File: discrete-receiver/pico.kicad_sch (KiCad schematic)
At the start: 38 parts, among them SW1 Reset, U6 RP2350A, U7 W25Q128JVS, U8 NCP1117-3.3_SOT223, Y1 ABM8-272-T3

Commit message: update schematic for peter
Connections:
- net Pico_USB_D+ renamed Pico_USB+
- net Pico_USB_D- renamed Pico_USB-
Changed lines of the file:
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@@
-		)
-	)
-	(global_label "Pico_USB_D+"
-		(shape bidirectional)
-		(at 270.51 67.31 0)
-		(fields_autoplaced yes)
-		(effects
-			(font
-				(size 1.27 1.27)
-				(thickness 0.1588)
-			)
-			(justify left)
-		)
-		(property "Intersheetrefs" "${INTERSHEET_REFS}"
-			(at 287.3065 67.31 0)
-			(hide yes)
-			(show_name no)
-			(do_not_autoplace no)
-			(effects
-				(font
-					(size 1.27 1.27)
-				)
-				(justify left)
-			)
 		)
 	)
@@
 		)
 	)
-	(global_label "Pico_USB_D-"
-		(shape bidirectional)
-		(at 270.51 69.85 0)
-		(fields_autoplaced yes)
-		(effects
-			(font
-				(size 1.27 1.27)
-				(thickness 0.1588)
-			)
-			(justify left)
-		)
-		(property "Intersheetrefs" "${INTERSHEET_REFS}"
-			(at 287.3065 69.85 0)
-			(hide yes)
-			(show_name no)
-			(do_not_autoplace no)
-			(effects
-				(font
-					(size 1.27 1.27)
-				)
-				(justify left)
-			)
-		)
-	)
 	(global_label "XIN"
 		(shape passive)
@@
 		)
 	)
+	(hierarchical_label "Pico_USB+"
+		(shape output)
+		(at 270.51 67.31 0)
+		(effects
+			(font
+				(size 1.27 1.27)
+			)
+			(justify left)
+		)
+	)
+	(hierarchical_label "Pico_USB-"
+		(shape output)
+		(at 270.51 69.85 0)
+		(effects
+			(font
+				(size 1.27 1.27)
+			)
+			(justify left)
+		)
+	)

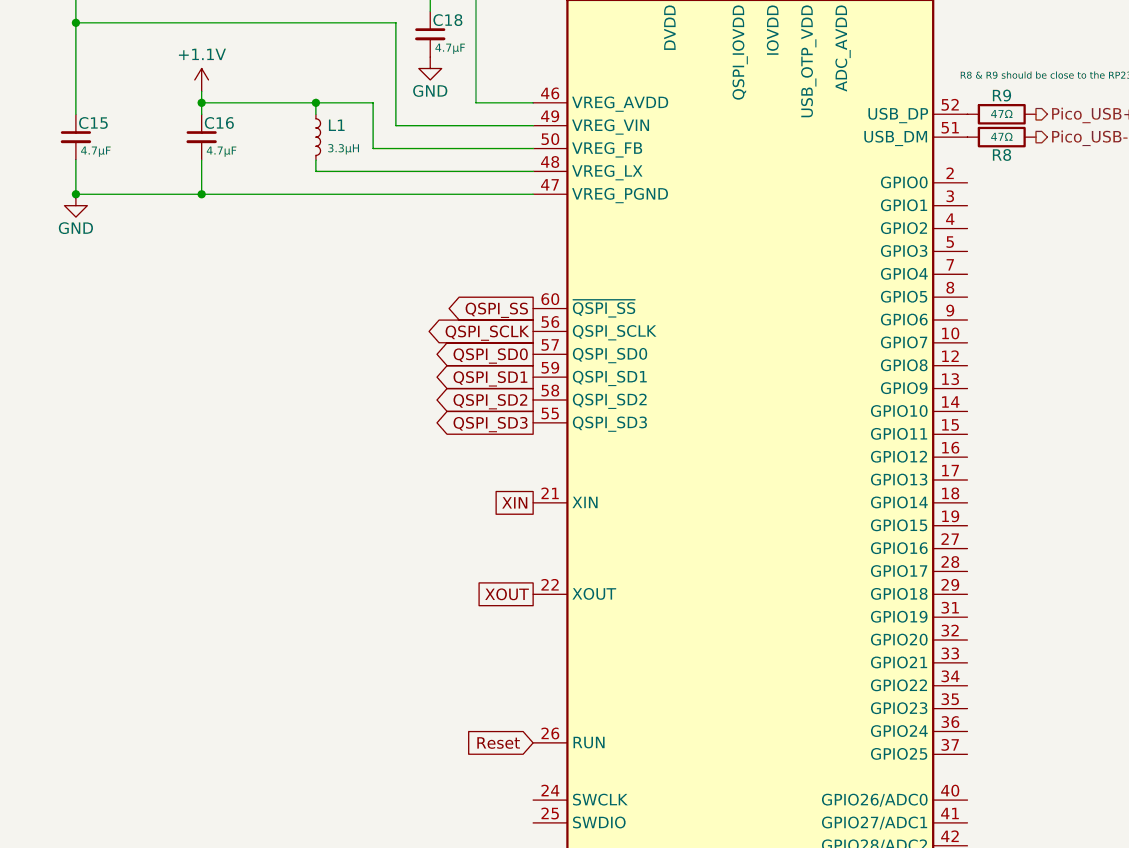
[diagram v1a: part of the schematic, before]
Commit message: updated schematic
clock generator, ADC, and 24.576 oscillator
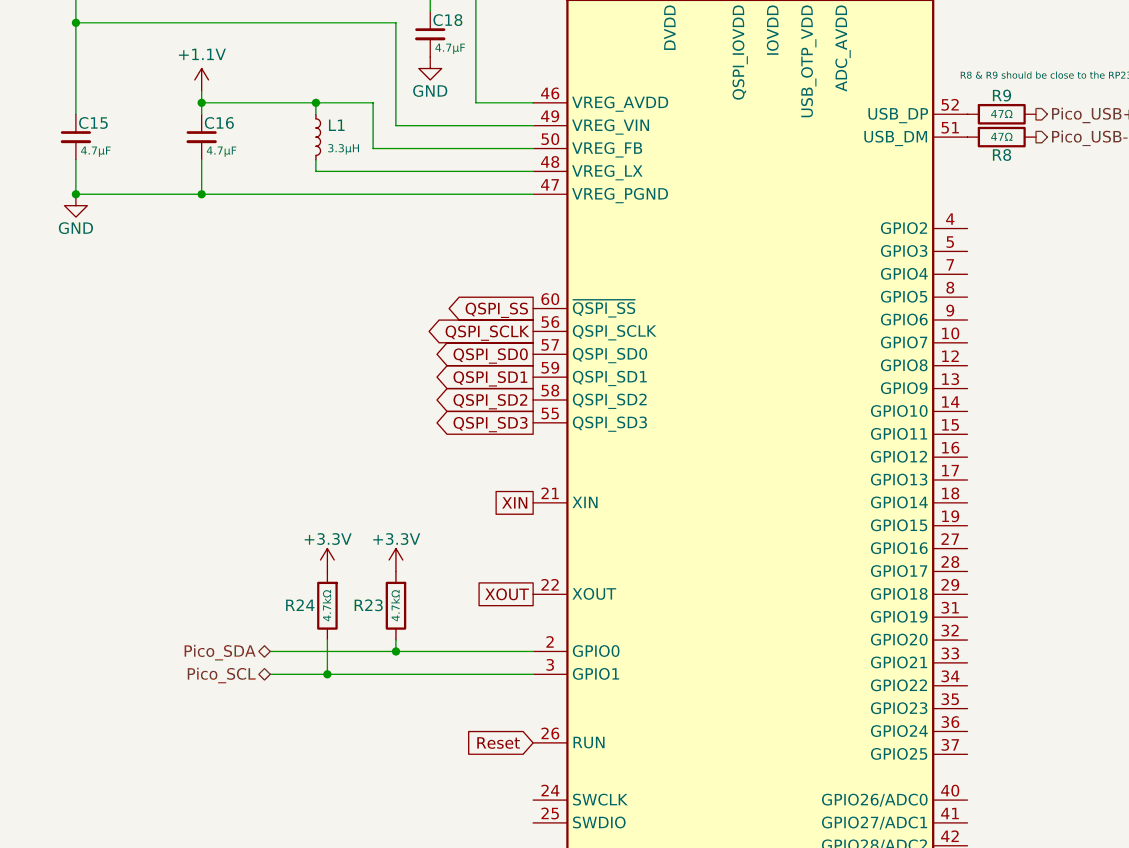
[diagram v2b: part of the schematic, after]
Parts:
- added R23, R24: 4.7kΩ, symbol Device:R
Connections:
- net +3.3V: now also R23.2, R24.2
- net Pico_SDA: now reaches U6.2 (GPIO0)
- net Pico_SDA: now also R23.1
- net Pico_SCL: now reaches U6.3 (GPIO1)
- net Pico_SCL: now also R24.1

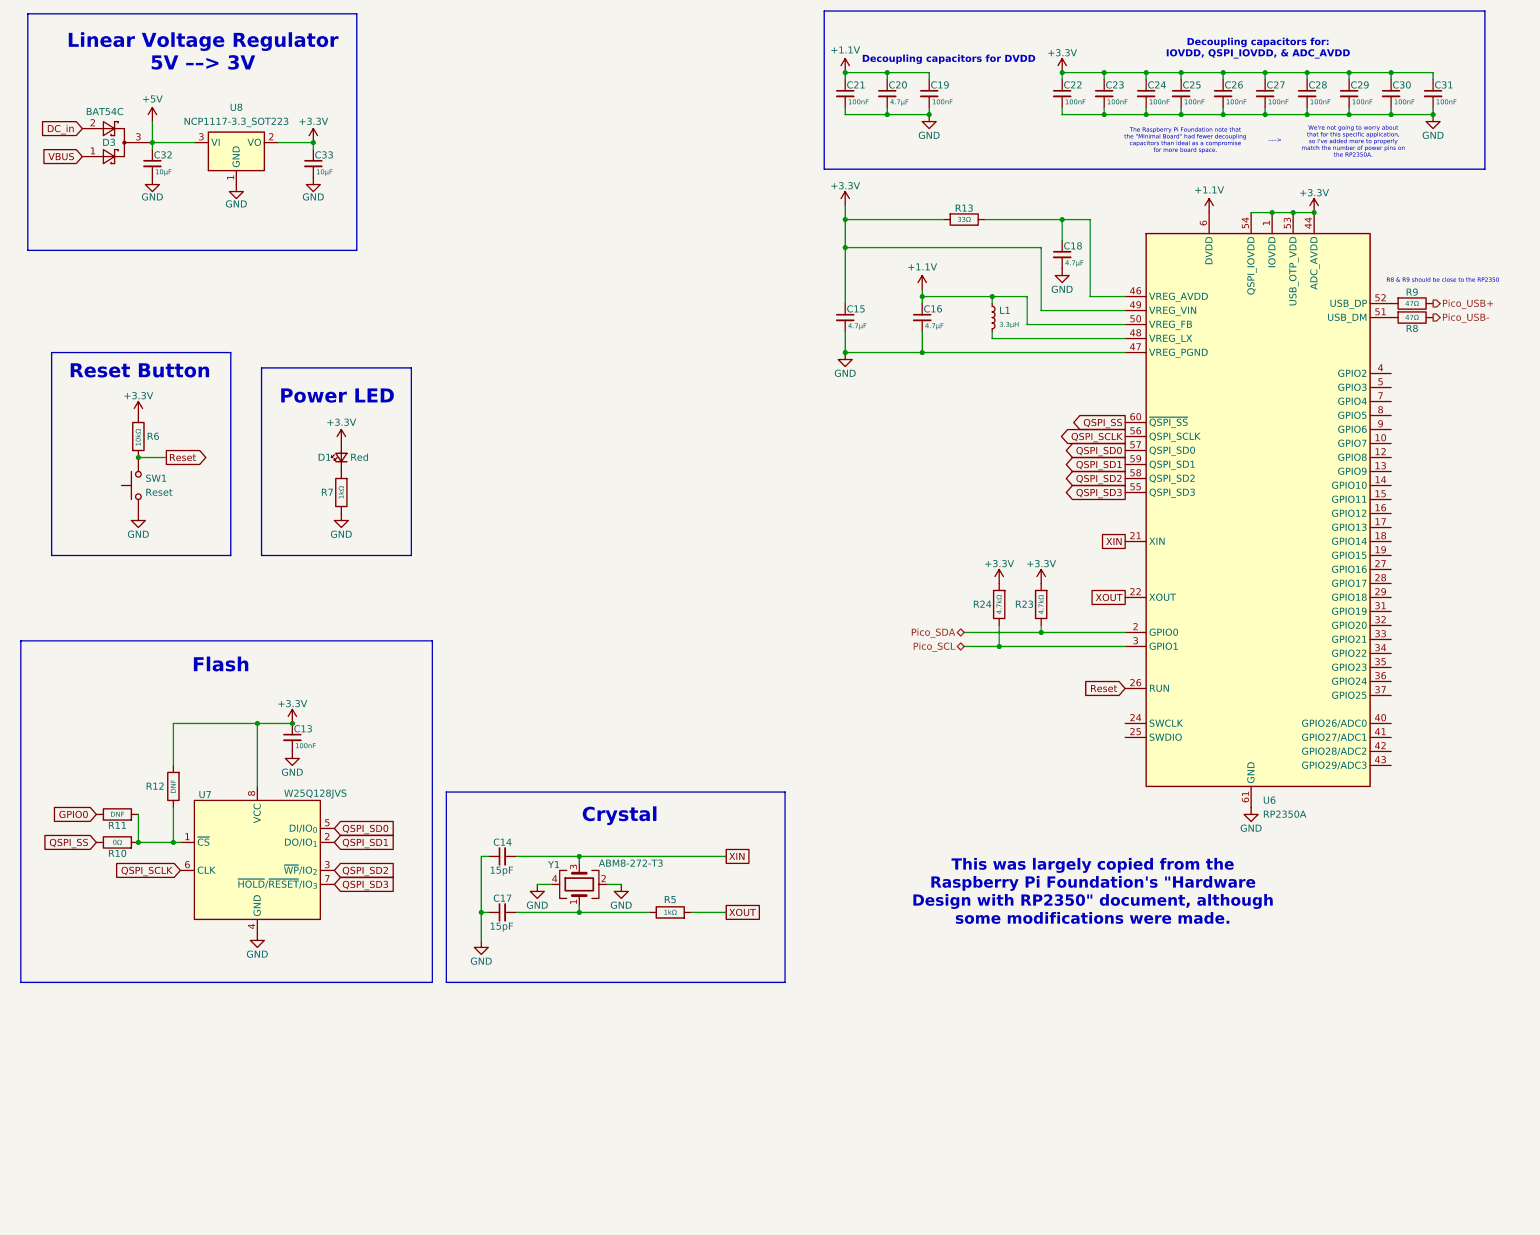
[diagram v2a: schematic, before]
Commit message: POE implemented, working on finishing Ethernet Implementation
I've added the SI-52003 rj45 jack with included magnetics, which is designed for POE and has outputs for such. The 4 power lines pass through two full bridge rectifiers to ensure the polarity of a 48V POE source, then that voltage is fed to an AG9905LP DC-DC converter. This module is designed to be low-noise, although still not perfect. By jumpering its ADJ pin to V- (GND), we can boost it's output voltage to 5.65V rather than 5V. Then, we can use a low-noise LDO regulator to filter the voltage as much as possible to create a good 5V source for the rest of the components on the board. Three LM66100 ICs are used as ideal diodes to select whichever of the three power sources has the highest voltage, and not allow backfeeding into the others. These three 5V power sources are USB, barrel jack, and POE. At this point all power sources pass through the TPS7A20, which is our 5V low-noise LDO regulator. That gives us the main 5V bus.
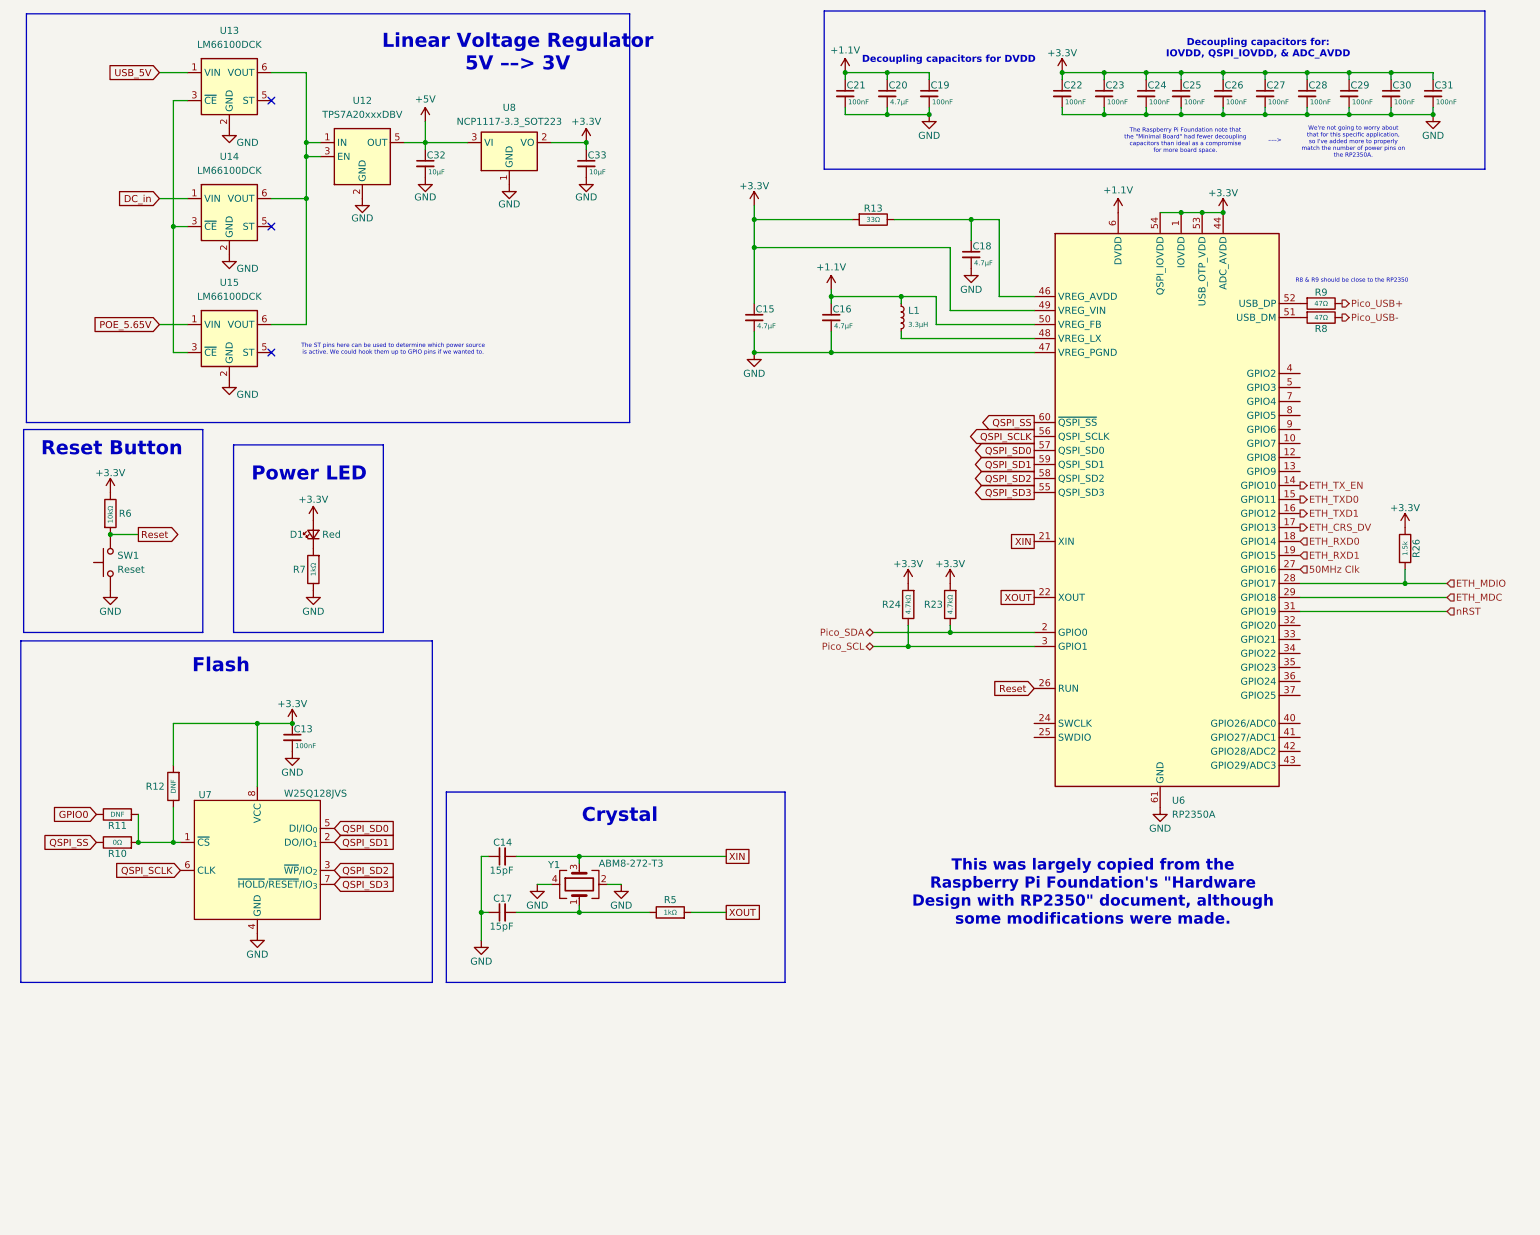
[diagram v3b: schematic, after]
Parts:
- removed D3: BAT54C, Package_TO_SOT_SMD:SOT-23, symbol Diode:BAT54C
- added R26: 1.5k, symbol Device:R
- added U12: TPS7A20xxxDBV, Package_TO_SOT_SMD:SOT-23-5, symbol Regulator_Linear:TPS7A20xxxDBV
- added U13, U14, U15: LM66100DCK, Package_TO_SOT_SMD:SOT-363_SC-70-6, symbol Power_Management:LM66100DCK
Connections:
- net +3.3V: now also R26.1
- net +5V: now also U12.5 (OUT)
- net DC_in: now also U14.1 (VIN)
- net GND: now also U12.2 (GND), U13.2 (GND), U14.2 (GND), U15.2 (GND)
- net ETH_TX_EN: now reaches U6.14 (GPIO10)
- net ETH_TXD0: now reaches U6.15 (GPIO11)
- net ETH_TXD1: now reaches U6.16 (GPIO12)
- net ETH_CRS_DV: now reaches U6.17 (GPIO13)
- net ETH_RXD0: now reaches U6.18 (GPIO14)
- net ETH_RXD1: now reaches U6.19 (GPIO15)
- net 50MHz Clk: now reaches U6.27 (GPIO16)
- net ETH_MDIO: now reaches U6.28 (GPIO17)
- net ETH_MDIO: now also R26.2
- net ETH_MDC: now reaches U6.29 (GPIO18)
- net nRST: now reaches U6.31 (GPIO19)
- new net: U13.3 (~{CE}), U14.3 (~{CE}), U15.3 (~{CE})
- new net: U12.1 (IN), U12.3 (EN), U13.6 (VOUT), U14.6 (VOUT), U15.6 (VOUT)
- new net POE_5.65V: U15.1 (VIN)
- new net USB_5V: U13.1 (VIN)
- no-connect marks 0 -> 3
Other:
- note added: "The ST pins here can be used to determine which power source is active. We could hook them up to GPIO pins if we wanted to."
- moved on the sheet: C15, C16, C18, C32, C33, D1, L1, R13, R23, R24, R6, R7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

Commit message: Fixed a couple bugs
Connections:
- net at U13.3 (~{CE}), U14.3 (~{CE}), U15.3 (~{CE}): now also U12.1 (IN), U12.3 (EN), U13.6 (VOUT), U14.6 (VOUT), U15.6 (VOUT)
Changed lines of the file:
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@@
+	)
+	(junction
+		(at 41.91 40.64)
+		(diameter 0)
+		(color 0 0 0 0)
 	)
 	(junction
@@
 	(wire
 		(pts
+			(xy 41.91 40.64) (xy 41.91 53.34)
+		)
+		(stroke
+			(width 0)
+			(type default)
+		)
+	)
+	(wire
+		(pts
 			(xy 171.45 33.02) (xy 179.07 33.02)
 		)
@@
 	(wire
 		(pts
+			(xy 41.91 40.64) (xy 66.04 40.64)
+		)
+		(stroke
+			(width 0)
+			(type default)
+		)
+	)
+	(wire
+		(pts
 			(xy 191.77 66.04) (xy 191.77 52.07)
 		)
@@
 	(wire
 		(pts
-			(xy 41.91 30.48) (xy 41.91 53.34)
+			(xy 41.91 30.48) (xy 41.91 40.64)
 		)
 		(stroke
@@
 		(in_pos_files yes)
 		(dnp no)
-		(fields_autoplaced yes)
 		(property "Reference" "U14"
-			(at 52.07 40.64 0)
+			(at 52.07 42.926 0)
 			(show_name no)
 			(do_not_autoplace no)
@@
 		)
 		(property "Value" "LM66100DCK"
-			(at 52.07 43.18 0)
-			(show_name no)
-			(do_not_autoplace no)
+			(at 52.07 44.704 0)
+			(show_name no)
+			(do_not_autoplace no)
